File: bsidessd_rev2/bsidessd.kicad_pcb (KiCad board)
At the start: 2 copper layers, 50 x 50 mm, 26 parts, among them J1 Conn_01x05, J2 Conn_01x05, J3 USB_B_Micro, SW1 PTS810, U1 ATSAMD21E18A-AUT, U2 AP2112K-3.3

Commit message: Passes DRC :) Need a sanity check before ordering.
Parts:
- removed C4: 1nF, Capacitor_SMD:C_0805_2012Metric
- removed D3, D5, D7, D8, D9: WS2812B, LED_SMD:LED_WS2812B_PLCC4_5.0x5.0mm_P3.2mm
- removed TP1: SWD, Connector_PinHeader_2.54mm:PinHeader_1x01_P2.54mm_Vertical
- removed TP2: SWC, Connector_PinHeader_2.54mm:PinHeader_1x01_P2.54mm_Vertical
- removed TP3: Battery, Connector_PinHeader_2.54mm:PinHeader_1x01_P2.54mm_Vertical
- removed TP4: Ground, Connector_PinHeader_2.54mm:PinHeader_1x01_P2.54mm_Vertical
- added BT1: 3xAAA Keystone 2479, Battery:BatteryHolder_Keystone_2479_3xAAA, B.Cu at (77.5, 139.0)
- added SW2: JS202011SCQN, andnxor:JS202011SCQN, B.Cu at (67.0, 134.0)
- added SW3: USER Button, Button_Switch_SMD:SW_SPST_PTS810, F.Cu at (123.5, 147.5)
- added TC1: Tag Connect 2050, andnxor:TC2050-IDC-FP-NoSilk, B.Cu at (139.0, 134.5)
- added U3: sk6812_side, andnxor:LED_SK6812_SIDE, F.Cu at (61.0, 122.5)
- added U4: sk6812_side, andnxor:LED_SK6812_SIDE, F.Cu at (80.5, 122.5)
- added U5: sk6812_side, andnxor:LED_SK6812_SIDE, F.Cu at (100.0, 122.5)
- added U6: sk6812_side, andnxor:LED_SK6812_SIDE, F.Cu at (118.0, 122.5)
- added U7: sk6812_side, andnxor:LED_SK6812_SIDE, F.Cu at (138.5, 122.5)
- added g1: graphic, bsidessd_rev2:bsidessd_rev2, F.Cu at (100.0, 100.0)
- C3, C5, D1, D4, J3, U2: moved to B.Cu
- J1: value Conn_01x05 -> Conn_01x09; footprint Connector_PinHeader_2.54mm:PinHeader_1x05_P2.54mm_Vertical -> Connector_PinHeader_2.54mm:PinHeader_1x09_P2.54mm_Vertical
- J2: value Conn_01x05 -> SWD; footprint Connector_PinHeader_2.54mm:PinHeader_1x05_P2.54mm_Vertical -> Connector_PinHeader_2.54mm:PinHeader_1x06_P2.54mm_Vertical
- SW1: value PTS810 -> RESET Button
- moved J3 143.6 mm to (52.8, 132.7), turned to 90 degrees
- moved D1 122.3 mm to (60.0, 123.0), turned to 180 degrees
- moved D4 121.9 mm to (60.0, 121.0), turned to 180 degrees
- moved C3 113.8 mm to (63.7, 120.1), turned to 90 degrees
- moved U2 109.4 mm to (67.0, 122.0), turned to 0 degrees
- moved C5 105.2 mm to (70.4, 123.9), turned to 270 degrees
- moved D2 104.5 mm to (80.5, 148.0), turned to 0 degrees
- moved R1 97.7 mm to (84.0, 148.0), turned to 0 degrees
- moved D6 90.0 mm to (77.0, 148.0)
- moved R2 90.0 mm to (73.5, 148.0)
- moved C2 86.8 mm to (92.0, 122.5), turned to 180 degrees
- moved SW1 82.0 mm to (116.5, 147.5), turned to 180 degrees
- moved J1 81.7 mm to (89.8, 148.0)
- moved U1 78.6 mm to (100.0, 131.0)
- moved C1 65.5 mm to (107.5, 122.5)
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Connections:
- net /D+ renamed USB_DP
- net /D- renamed USB_DM
- J1 pad 2: GND -> +3V3
- J1 pad 3: /D4_A2_PAU06_TXD_MOSI -> GND
- J1 pad 4: /D3_A3_PAU07_RXD_SCK -> /D4_A2_PAU06_TXD_MOSI
- J1 pad 5: /~RESET -> /D3_A3_PAU07_RXD_SCK
- J2 pad 2: /D2_A1_PAU09_SCL_MISO -> SWDIO
- J2 pad 3: /D1_A0_PAU02 -> SWCLK
- J2 pad 4: /D0_A4_PAU08_SDA -> VBUS
- J2 pad 5: VBUS -> /~RESET
- SW1 pad 1: /~RESET -> GND
- SW1 pad 2: GND -> /~RESET
- U1 pad 1: /LED -> LED
- U1 pad 31: Net-(TP2-Pad1) -> SWCLK
- U1 pad 32: Net-(TP1-Pad1) -> SWDIO
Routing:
- net +3V3: track 2.93 -> 232.5 mm, vias 0 -> 4
- net SWCLK: track 0.00 -> 96.3 mm
- net SWDIO: track 0.00 -> 95.9 mm
- net /~RESET: track 27.3 -> 101.7 mm
- net VBUS: track 68.7 -> 129.0 mm, vias 3 -> 4
- net /D1_A0_PAU02: track 22.0 -> 65.3 mm
- net LED: track 0.00 -> 37.9 mm, vias 0 -> 2
- net GND: track 42.0 -> 71.1 mm, vias 13 -> 15
- net Net-(U3-Pad3): track 0.00 -> 28.8 mm, vias 0 -> 2
- net Net-(U5-Pad3): track 0.00 -> 27.4 mm, vias 0 -> 2
- net Net-(U6-Pad3): track 0.00 -> 25.2 mm
- net Net-(U4-Pad3): track 0.00 -> 24.4 mm, vias 0 -> 2
- net /LED: track 21.8 -> 0.00 mm, vias 2 -> 0
- net Net-(R1-Pad2): track 3.91 -> 25.0 mm, vias 0 -> 2
- net Net-(BT1-Pad1): track 0.00 -> 18.5 mm, vias 0 -> 1
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- removed copper zone on F.Cu, net +3V3
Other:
- board size 50 x 50 mm -> 97 x 43.3 mm
- net class Default: clearance 0.1524 -> 0.2; trace_width 0.1524 -> 0.2
- rule trace_clearance: 0.1524 -> 0.2

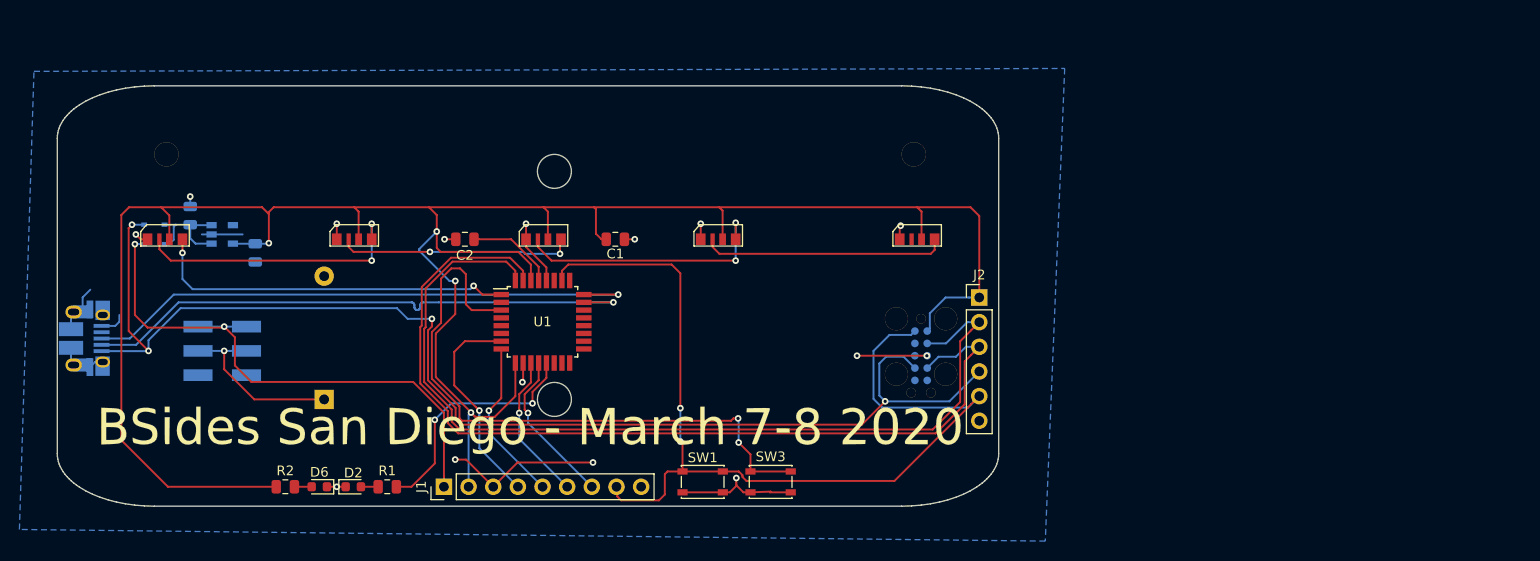
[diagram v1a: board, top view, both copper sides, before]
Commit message: Cleaned up traces and silk. Ordered rev2 boards.
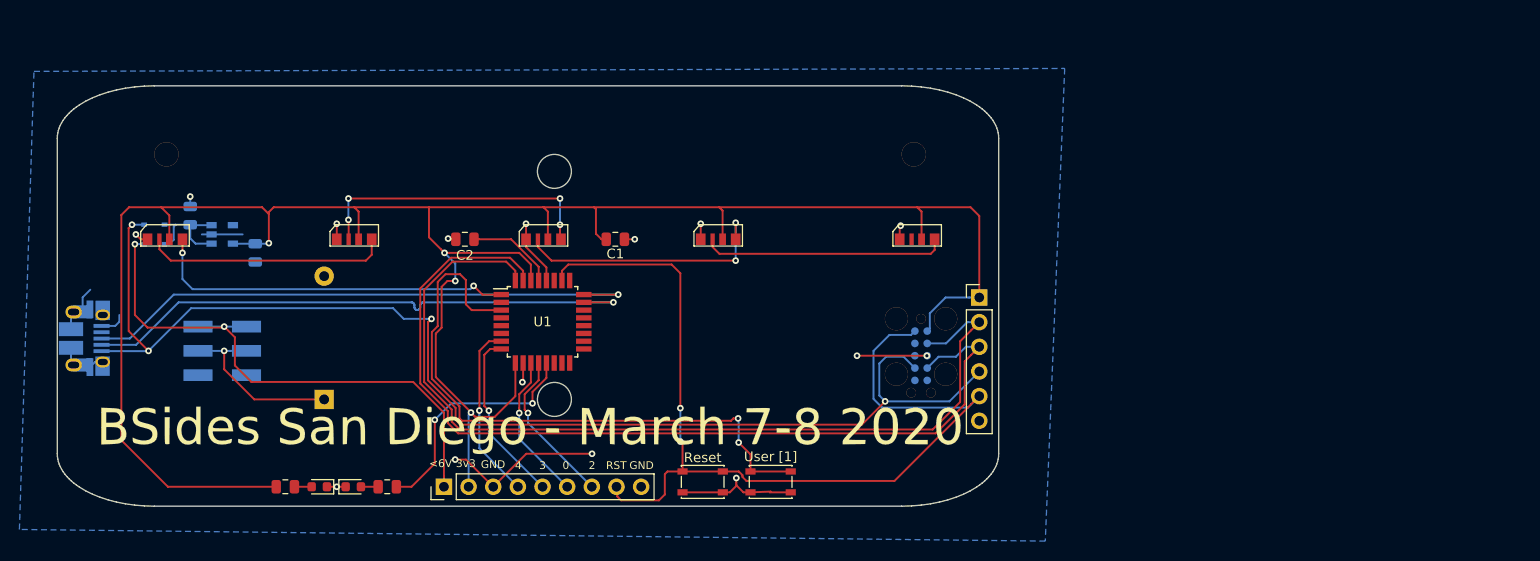
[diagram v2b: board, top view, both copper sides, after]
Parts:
- removed SW3: USER Button, Button_Switch_SMD:SW_SPST_PTS810
- added User [1]: USER Button, Button_Switch_SMD:SW_SPST_PTS810, F.Cu at (123.5, 147.5)
- renumbered SW1 to Reset
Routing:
- net Net-(U4-Pad3): track 24.4 -> 30.3 mm, vias 2 -> 4
- net +3V3: track 232.5 -> 228.4 mm
- net /D4_A2_PAU06_TXD_MOSI: track 21.9 -> 18.3 mm
- net Net-(U3-Pad3): track 28.8 -> 25.2 mm, vias 2 -> 0
- net /D3_A3_PAU07_RXD_SCK: track 17.0 -> 18.1 mm
- net /D1_A0_PAU02: track 65.3 -> 64.4 mm
- net VBUS: track 129.0 -> 128.3 mm
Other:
- board text added: ""Trinket M0" clone Circuit Python 5.0 Plug into USB Do not edit files directly on the badge"
- board text added: "0"
- board text added: "2"
- board text added: "3"
- board text added: "3v3"
- board text added: "4"
- board text added: "<6V"
- board text added: "GND"
- board text added: "Getting Started"
- board text added: "On/Off"
- board text added: "RST"
